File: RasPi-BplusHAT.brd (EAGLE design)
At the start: 65 x 56 mm, 7 parts, among them K1 PIN20X2, U1 EEPROM24

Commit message: delete cruft
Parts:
- removed C1: 100nF, resistor:C0805K
- removed CFG: (no value), FLYFISH:PIN_W_2
- removed R1, R2: 3k9, resistor:M0805
- removed R3: 1k, resistor:M0805
- removed U1: EEPROM24, FLYFISH:SOIC8
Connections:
- removed net N$1: K1.28, R1.1, U1.6
- removed net N$2: K1.27, R2.1, U1.5
- removed net N$3: CFG.1, R3.1, U1.7
- net +3V3: no longer C1.1, R1.2, R2.2, R3.2, U1.8
- net GND: no longer C1.2, CFG.2, U1.1, U1.2, U1.3, U1.4
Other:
- board text removed: "BOTTOM"
- board text removed: "TOP"
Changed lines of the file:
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@@
 <hole x="61.5" y="52.5" drill="2.8"/>
 <hole x="61.5" y="3.5" drill="2.8"/>
-<text x="49.09" y="1.335" size="1.143" layer="1" font="vector" ratio="23" rot="SR0" align="center">TOP</text>
-<text x="49.09" y="1.335" size="1.143" layer="16" font="vector" ratio="23" rot="SMR0" align="center">BOTTOM</text>
 <circle x="3.5" y="52.5" radius="1.55" width="3.1" layer="41"/>
 <circle x="61.5" y="52.5" radius="1.55" width="3.1" layer="41"/>
@@
 <wire x1="45" y1="20" x2="46" y2="19" width="0" layer="46" curve="-90"/>
 <wire x1="46" y1="19" x2="46" y2="4" width="0" layer="46"/>
-<wire x1="44" y1="19" x2="44" y2="4" width="0" layer="20"/>
-<wire x1="46" y1="19" x2="46" y2="4" width="0" layer="20"/>
-<wire x1="45" y1="20" x2="46" y2="19" width="0" layer="20" curve="-90"/>
-<wire x1="45" y1="20" x2="44" y2="19" width="0" layer="20" curve="90"/>
-<wire x1="46" y1="4" x2="45" y2="3" width="0" layer="20" curve="-90"/>
-<wire x1="44" y1="4" x2="45" y2="3" width="0" layer="20" curve="90"/>
 </plain>
 <attributes>
@@
 <attribute name="VALUE" x="45.2" y="48.309" size="1.27" layer="27" ratio="10"/>
 </element>
-<element name="U1" library="FLYFISH" package="SOIC8" value="EEPROM24" x="58.535" y="37.26" smashed="yes" rot="R90">
-<attribute name="NAME" x="55.0425" y="39.927" size="1.016" layer="25" ratio="10"/>
-<attribute name="VALUE" x="57.265" y="39.9905" size="0.8128" layer="27"/>
-</element>
-<element name="R1" library="resistor" package="M0805" value="3k9" x="61.075" y="42.0225" smashed="yes">
-<attribute name="TOLERANCE" value="5%" x="61.075" y="42.0225" size="1.778" layer="27" display="off"/>
-<attribute name="NAME" x="63.07525" y="41.92725" size="1.016" layer="25" ratio="10"/>
-<attribute name="VALUE" x="62.9165" y="41.0065" size="0.8128" layer="27"/>
-</element>
-<element name="C1" library="resistor" package="C0805K" value="100nF" x="61.075" y="32.4975" smashed="yes">
-<attribute name="DIELECTRIC" value="X7R" x="61.075" y="32.4975" size="1.778" layer="27" display="off"/>
-<attribute name="NAME" x="59.17" y="33.60875" size="1.016" layer="25" ratio="10"/>
-<attribute name="VALUE" x="61.0275" y="33.7675" size="0.8128" layer="27"/>
-</element>
-<element name="R2" library="resistor" package="M0805" value="3k9" x="61.075" y="44.5625" smashed="yes">
-<attribute name="TOLERANCE" value="5%" x="61.075" y="44.5625" size="1.778" layer="27" display="off"/>
-<attribute name="NAME" x="63.07525" y="44.46725" size="1.016" layer="25" ratio="10"/>
-<attribute name="VALUE" x="62.9165" y="43.5465" size="0.8128" layer="27"/>
-</element>
-<element name="R3" library="resistor" package="M0805" value="1k" x="55.995" y="32.4975" smashed="yes">
-<attribute name="TOLERANCE" value="5%" x="55.995" y="32.4975" size="1.778" layer="27" display="off"/>
-<attribute name="NAME" x="54.18525" y="33.60875" size="1.016" layer="25" ratio="10"/>
-<attribute name="VALUE" x="56.40775" y="33.7675" size="0.8128" layer="27"/>
-</element>
-<element name="CFG" library="FLYFISH" package="PIN_W_2" value="" x="59.485" y="29.73" smashed="yes" rot="R90">
-<attribute name="NAME" x="54.3313" y="29.08755" size="1.4224" layer="25" ratio="15"/>
-<attribute name="VALUE" x="65.2" y="28.46" size="1.27" layer="27" rot="R90"/>
-</element>
 </elements>
 <signals>
@@
 </signal>
 <signal name="GND">
-<contactref element="U1" pad="4"/>
-<contactref element="U1" pad="3"/>
-<contactref element="U1" pad="1"/>
-<contactref element="U1" pad="2"/>
-<contactref element="CFG" pad="2"/>
-<contactref element="C1" pad="2"/>
 <contactref element="K1" pad="9"/>
 <contactref element="K1" pad="25"/>
@@
 <vertex x="0" y="18.5"/>
 </polygon>
+<wire x1="49.01" y1="53.77" x2="56.63" y2="51.23" width="0" layer="19" extent="1-1"/>
+<wire x1="43.93" y1="53.77" x2="49.01" y2="53.77" width="0" layer="19" extent="1-1"/>
+<wire x1="38.85" y1="51.23" x2="43.93" y2="53.77" width="0" layer="19" extent="1-1"/>
+<wire x1="31.23" y1="53.77" x2="38.85" y2="51.23" width="0" layer="19" extent="1-1"/>
+<wire x1="23.61" y1="53.77" x2="31.23" y2="53.77" width="0" layer="19" extent="1-1"/>
+<wire x1="18.53" y1="51.23" x2="23.61" y2="53.77" width="0" layer="19" extent="1-1"/>
+<wire x1="13.45" y1="53.77" x2="18.53" y2="51.23" width="0" layer="19" extent="1-1"/>
 </signal>
 <signal name="+3V3">
-<contactref element="U1" pad="8"/>
-<contactref element="R3" pad="2"/>
-<contactref element="C1" pad="1"/>
-<contactref element="R2" pad="2"/>
-<contactref element="R1" pad="2"/>
 <contactref element="K1" pad="1"/>
 <contactref element="K1" pad="17"/>
-<wire x1="62.025" y1="42.0225" x2="62.025" y2="44.5625" width="0" layer="19" extent="1-1"/>
-<wire x1="55.205" y1="35.355" x2="62.025" y2="42.0225" width="0" layer="19" extent="1-1"/>
-<wire x1="56.945" y1="32.4975" x2="55.205" y2="35.355" width="0" layer="19" extent="1-1"/>
-<wire x1="60.075" y1="32.4975" x2="56.945" y2="32.4975" width="0" layer="19" extent="1-1"/>
-<wire x1="28.69" y1="51.23" x2="55.205" y2="35.355" width="0" layer="19" extent="1-1"/>
 <wire x1="8.37" y1="51.23" x2="28.69" y2="51.23" width="0" layer="19" extent="1-1"/>
 </signal>
-<signal name="N$1">
-<contactref element="U1" pad="6"/>
-<contactref element="R1" pad="1"/>
-<contactref element="K1" pad="28"/>
-<wire x1="55.205" y1="37.895" x2="60.125" y2="42.0225" width="0" layer="19" extent="1-1"/>
-<wire x1="41.39" y1="53.77" x2="55.205" y2="37.895" width="0" layer="19" extent="1-1"/>
-</signal>
-<signal name="N$2">
-<contactref element="U1" pad="5"/>
-<contactref element="R2" pad="1"/>
-<contactref element="K1" pad="27"/>
-<wire x1="55.205" y1="39.165" x2="60.125" y2="44.5625" width="0" layer="19" extent="1-1"/>
-<wire x1="41.39" y1="51.23" x2="55.205" y2="39.165" width="0" layer="19" extent="1-1"/>
-</signal>
-<signal name="N$3">
-<contactref element="U1" pad="7"/>
-<contactref element="R3" pad="1"/>
-<contactref element="CFG" pad="1"/>
-<wire x1="55.045" y1="32.4975" x2="55.205" y2="36.625" width="0" layer="19" extent="1-1"/>
-<wire x1="59.485" y1="29.73" x2="55.045" y2="32.4975" width="0" layer="19" extent="1-1"/>
-</signal>
 <signal name="+5V">

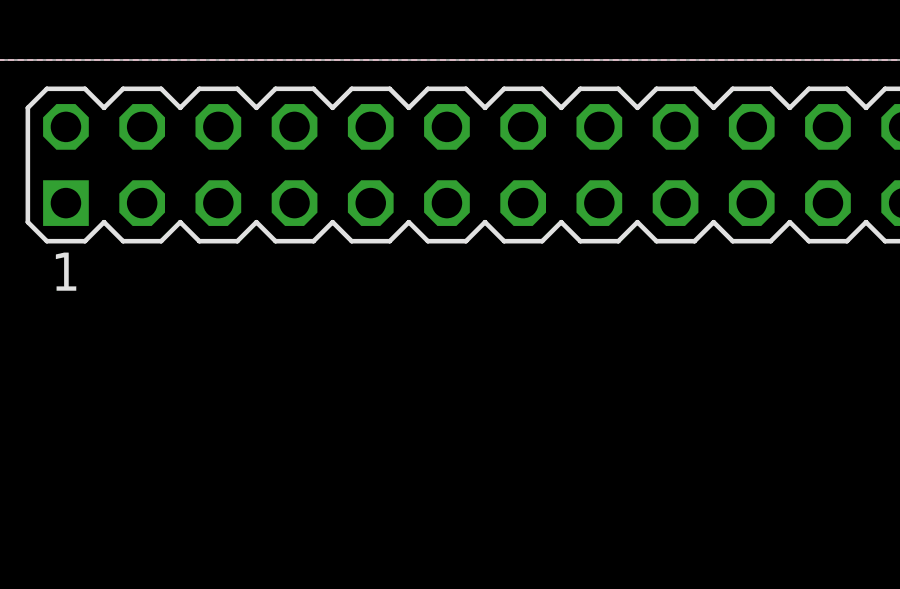
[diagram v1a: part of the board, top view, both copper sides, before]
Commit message: add pin labels to raspi header
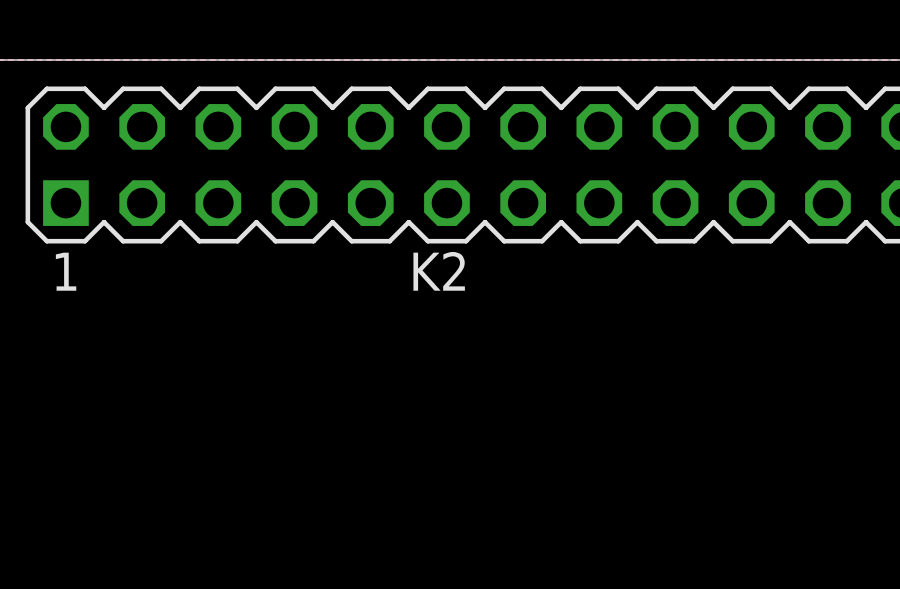
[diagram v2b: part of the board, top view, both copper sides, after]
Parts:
- removed K1: PIN20X2, FLYFISH:PIN_20X2
- added K2: RASPI_HEADER, RasPi-BplusHAT:RASPI_HEADER
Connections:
- net +3V3: now also K2.3.3V@17, K2.3V3; no longer K1.1, K1.17
- net +5V: now also K2.5V@2, K2.5V@4; no longer K1.2, K1.4
- net GND: now also K2.GND@14, K2.GND@20, K2.GND@25, K2.GND@30, K2.GND@34, K2.GND@39, K2.GND@6, K2.GND@9; no longer K1.14, K1.20, K1.25, K1.30, K1.34, K1.39, K1.6, K1.9
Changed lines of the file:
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@@
 <setting verticaltext="up"/>
 </settings>
-<grid distance="1" unitdist="mm" unit="mm" style="lines" multiple="1" display="yes" altdistance="0.025" altunitdist="inch" altunit="inch"/>
+<grid distance="0.5" unitdist="mm" unit="mm" style="lines" multiple="1" display="yes" altdistance="0.025" altunitdist="inch" altunit="inch"/>
 <layers>
 <layer number="1" name="Top" color="4" fill="1" visible="yes" active="yes"/>
@@
 <layer number="54" name="bGND_GNDA" color="7" fill="1" visible="no" active="no"/>
 <layer number="56" name="wert" color="7" fill="1" visible="no" active="no"/>
+<layer number="90" name="Modules" color="5" fill="1" visible="no" active="no"/>
 <layer number="91" name="Nets" color="2" fill="1" visible="no" active="no"/>
 <layer number="92" name="Busses" color="1" fill="1" visible="no" active="no"/>
@@
 <layer number="97" name="Info" color="7" fill="1" visible="no" active="no"/>
 <layer number="98" name="Guide" color="6" fill="1" visible="no" active="no"/>
+<layer number="100" name="NonViaHole" color="7" fill="1" visible="yes" active="yes"/>
+<layer number="101" name="PlacementGuide" color="7" fill="1" visible="yes" active="yes"/>
+<layer number="102" name="TopSilkscreen" color="7" fill="1" visible="yes" active="yes"/>
+<layer number="103" name="not_populated" color="7" fill="1" visible="yes" active="yes"/>
+<layer number="104" name="BottomSilkscreen" color="7" fill="1" visible="yes" active="yes"/>
+<layer number="105" name="tPlate" color="7" fill="1" visible="yes" active="yes"/>
+<layer number="106" name="bPlate" color="7" fill="1" visible="yes" active="yes"/>
+<layer number="107" name="Crop" color="7" fill="1" visible="yes" active="yes"/>
+<layer number="116" name="Patch_BOT" color="7" fill="1" visible="yes" active="yes"/>
+<layer number="121" name="_tsilk" color="7" fill="1" visible="yes" active="yes"/>
+<layer number="122" name="_bsilk" color="7" fill="1" visible="yes" active="yes"/>
+<layer number="144" name="Drill_legend" color="7" fill="1" visible="yes" active="yes"/>
+<layer number="151" name="HeatSink" color="7" fill="1" visible="yes" active="yes"/>
+<layer number="200" name="200bmp" color="7" fill="1" visible="yes" active="yes"/>
+<layer number="201" name="201bmp" color="7" fill="1" visible="yes" active="yes"/>
+<layer number="202" name="202bmp" color="7" fill="1" visible="yes" active="yes"/>
+<layer number="203" name="203bmp" color="7" fill="1" visible="yes" active="yes"/>
+<layer number="204" name="204bmp" color="7" fill="1" visible="yes" active="yes"/>
+<layer number="205" name="205bmp" color="7" fill="1" visible="yes" active="yes"/>
+<layer number="206" name="206bmp" color="7" fill="1" visible="yes" active="yes"/>
+<layer number="207" name="207bmp" color="7" fill="1" visible="yes" active="yes"/>
+<layer number="208" name="208bmp" color="7" fill="1" visible="yes" active="yes"/>
+<layer number="250" name="Descript" color="7" fill="1" visible="yes" active="yes"/>
+<layer number="251" name="SMDround" color="7" fill="1" visible="yes" active="yes"/>
+<layer number="254" name="cooling" color="7" fill="1" visible="yes" active="yes"/>
 </layers>
 <board>
@@
 </autorouter>
 <elements>
-<element name="K1" library="FLYFISH" package="PIN_20X2" value="PIN20X2" x="32.5" y="52.5" smashed="yes">
-<attribute name="VALUE" x="45.2" y="48.309" size="1.27" layer="27" ratio="10"/>
-</element>
+<element name="K2" library="RasPi-BplusHAT" package="RASPI_HEADER" value="RASPI_HEADER" x="32.5" y="52.5"/>
 </elements>
 <signals>
@@
 </signal>
 <signal name="GND">
-<contactref element="K1" pad="9"/>
-<contactref element="K1" pad="25"/>
-<contactref element="K1" pad="39"/>
-<contactref element="K1" pad="6"/>
-<contactref element="K1" pad="14"/>
-<contactref element="K1" pad="20"/>
-<contactref element="K1" pad="30"/>
-<contactref element="K1" pad="34"/>
 <polygon width="0.254" layer="16">
 <vertex x="0" y="3" curve="90"/>
@@
 <vertex x="0" y="18.5"/>
 </polygon>
+<contactref element="K2" pad="GND@9"/>
+<contactref element="K2" pad="GND@25"/>
+<contactref element="K2" pad="GND@39"/>
+<contactref element="K2" pad="GND@6"/>
+<contactref element="K2" pad="GND@14"/>
+<contactref element="K2" pad="GND@20"/>
+<contactref element="K2" pad="GND@30"/>
+<contactref element="K2" pad="GND@34"/>
 <wire x1="49.01" y1="53.77" x2="56.63" y2="51.23" width="0" layer="19" extent="1-1"/>
 <wire x1="43.93" y1="53.77" x2="49.01" y2="53.77" width="0" layer="19" extent="1-1"/>
@@
 </signal>
 <signal name="+3V3">
-<contactref element="K1" pad="1"/>
-<contactref element="K1" pad="17"/>
+<contactref element="K2" pad="3V3"/>
+<contactref element="K2" pad="3.3V@17"/>
 <wire x1="8.37" y1="51.23" x2="28.69" y2="51.23" width="0" layer="19" extent="1-1"/>
 </signal>
 <signal name="+5V">
-<contactref element="K1" pad="2"/>
-<contactref element="K1" pad="4"/>
+<contactref element="K2" pad="5V@2"/>
+<contactref element="K2" pad="5V@4"/>
 <wire x1="8.37" y1="53.77" x2="10.91" y2="53.77" width="0" layer="19" extent="1-1"/>
 </signal>

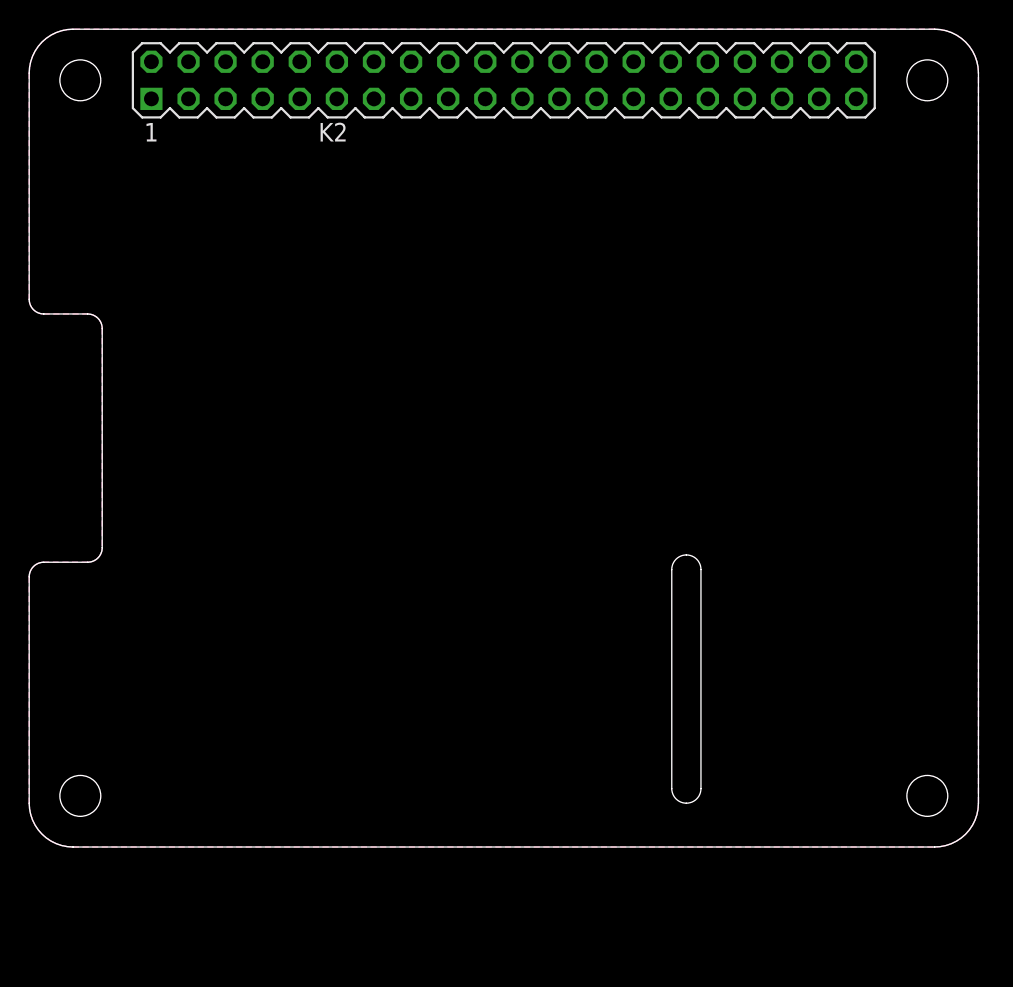
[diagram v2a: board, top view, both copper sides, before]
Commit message: add db15 and labeled nets
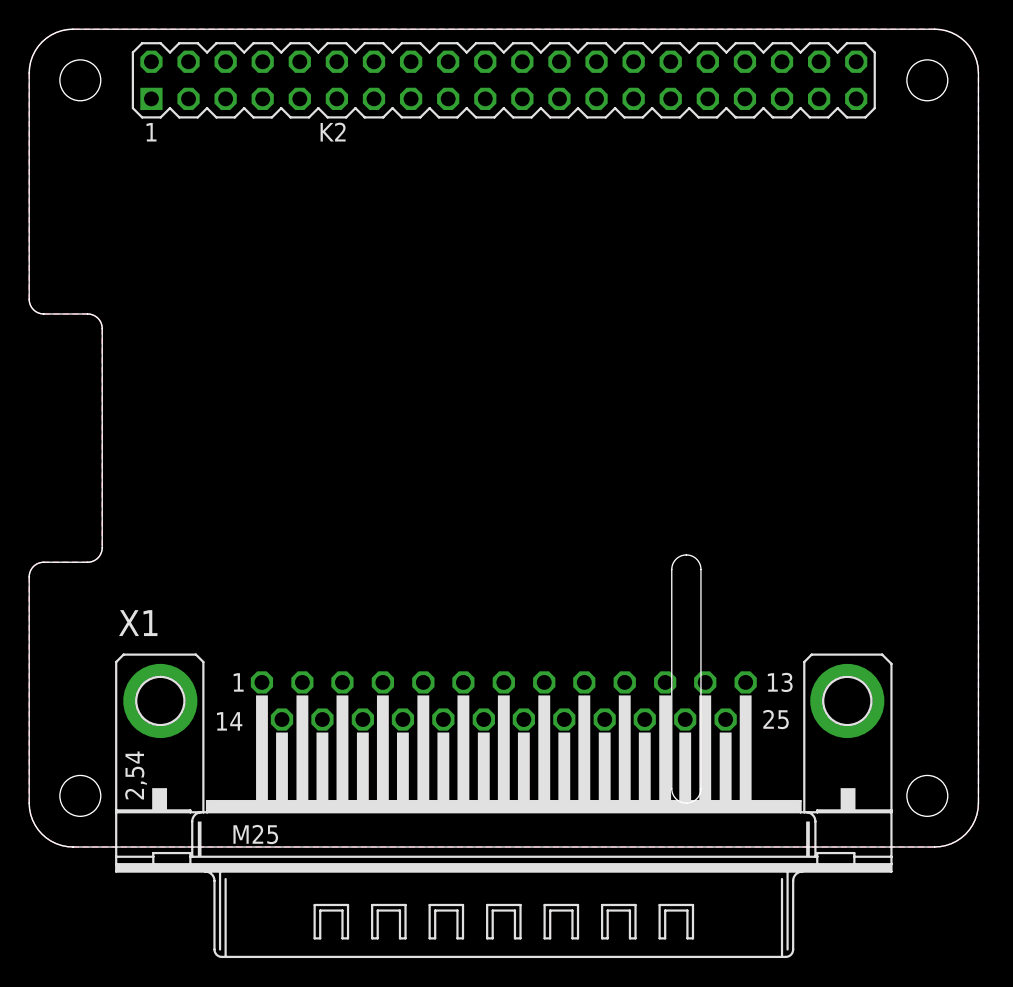
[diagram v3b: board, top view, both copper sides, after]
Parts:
- added X1: (no value), con-subd:M25HP
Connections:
- new net ANALOG1: X1.1
- new net ANALOG14: X1.14
- new net ANALOG15: X1.15
- new net ANALOG16: X1.16
- new net ANALOG17: X1.17
- new net ANALOG2: X1.2
- new net ANALOG3: X1.3
- new net ANALOG4: X1.4
- new net DIGI22: X1.22
- new net DIGI23: X1.23
- new net DIGI24: X1.24
- new net DIGIN10: X1.10
- new net DIGIN11: X1.11
- new net DIGIN12: X1.12
- new net DIGIN13: X1.13
- new net DIGIN9: X1.9
- new net DIGO18: X1.18
- new net DIGO19: X1.19
- new net DIGO20: X1.20
- new net DIGO21: X1.21
- new net DIGO5: X1.5
- new net DIGO6: X1.6
- new net DIGO7: X1.7
- new net DIGO8: X1.8
- net GND: now also X1.25
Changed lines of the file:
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@@
 <elements>
 <element name="K2" library="RasPi-BplusHAT" package="RASPI_HEADER" value="RASPI_HEADER" x="32.5" y="52.5"/>
+<element name="X1" library="con-subd" package="M25HP" value="" x="32.5" y="10">
+<attribute name="OC_NEWARK" value="unknown" x="32.5" y="10" size="1.778" layer="27" display="off"/>
+<attribute name="MPN" value="" x="32.5" y="10" size="1.778" layer="27" display="off"/>
+<attribute name="MF" value="" x="32.5" y="10" size="1.778" layer="27" display="off"/>
+<attribute name="OC_FARNELL" value="unknown" x="32.5" y="10" size="1.778" layer="27" display="off"/>
+</element>
 </elements>
 <signals>
@@
 <contactref element="K2" pad="GND@30"/>
 <contactref element="K2" pad="GND@34"/>
+<contactref element="X1" pad="25"/>
 <wire x1="49.01" y1="53.77" x2="56.63" y2="51.23" width="0" layer="19" extent="1-1"/>
 <wire x1="43.93" y1="53.77" x2="49.01" y2="53.77" width="0" layer="19" extent="1-1"/>
@@
 <wire x1="18.53" y1="51.23" x2="23.61" y2="53.77" width="0" layer="19" extent="1-1"/>
 <wire x1="13.45" y1="53.77" x2="18.53" y2="51.23" width="0" layer="19" extent="1-1"/>
+<wire x1="47.6892" y1="8.73" x2="38.85" y2="51.23" width="0" layer="19" extent="1-1"/>
 </signal>
 <signal name="+3V3">
@@
 <wire x1="8.37" y1="53.77" x2="10.91" y2="53.77" width="0" layer="19" extent="1-1"/>
 </signal>
+<signal name="ANALOG1">
+<contactref element="X1" pad="1"/>
+</signal>
+<signal name="ANALOG2">
+<contactref element="X1" pad="2"/>
+</signal>
+<signal name="ANALOG3">
+<contactref element="X1" pad="3"/>
+</signal>
+<signal name="ANALOG4">
+<contactref element="X1" pad="4"/>
+</signal>
+<signal name="DIGO5">
+<contactref element="X1" pad="5"/>
+</signal>
+<signal name="DIGO6">
+<contactref element="X1" pad="6"/>
+</signal>
+<signal name="DIGO7">
+<contactref element="X1" pad="7"/>
+</signal>
+<signal name="DIGO8">
+<contactref element="X1" pad="8"/>
+</signal>
+<signal name="DIGIN9">
+<contactref element="X1" pad="9"/>
+</signal>
+<signal name="DIGIN10">
+<contactref element="X1" pad="10"/>
+</signal>
+<signal name="DIGIN12">
+<contactref element="X1" pad="12"/>
+</signal>
+<signal name="DIGIN13">
+<contactref element="X1" pad="13"/>
+</signal>
+<signal name="ANALOG14">
+<contactref element="X1" pad="14"/>
+</signal>
+<signal name="ANALOG15">
+<contactref element="X1" pad="15"/>
+</signal>
+<signal name="ANALOG16">
+<contactref element="X1" pad="16"/>
+</signal>
+<signal name="ANALOG17">
+<contactref element="X1" pad="17"/>
+</signal>
+<signal name="DIGO18">
+<contactref element="X1" pad="18"/>
+</signal>
+<signal name="DIGO19">
+<contactref element="X1" pad="19"/>
+</signal>
+<signal name="DIGO20">
+<contactref element="X1" pad="20"/>
+</signal>
+<signal name="DIGO21">
+<contactref element="X1" pad="21"/>
+</signal>
+<signal name="DIGI22">
+<contactref element="X1" pad="22"/>
+</signal>
+<signal name="DIGI23">
+<contactref element="X1" pad="23"/>
+</signal>
+<signal name="DIGI24">
+<contactref element="X1" pad="24"/>
+</signal>
+<signal name="DIGIN11">
+<contactref element="X1" pad="11"/>
+</signal>
 </signals>
